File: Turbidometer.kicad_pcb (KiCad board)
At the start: 2 copper layers, 35 x 35 mm, 16 parts, among them IC1 BH1730FVC-TR, IC2 NLSX4373DR2G, J1 Conn_01x04, J2 Conn_01x04, U1 LP2985-3.0

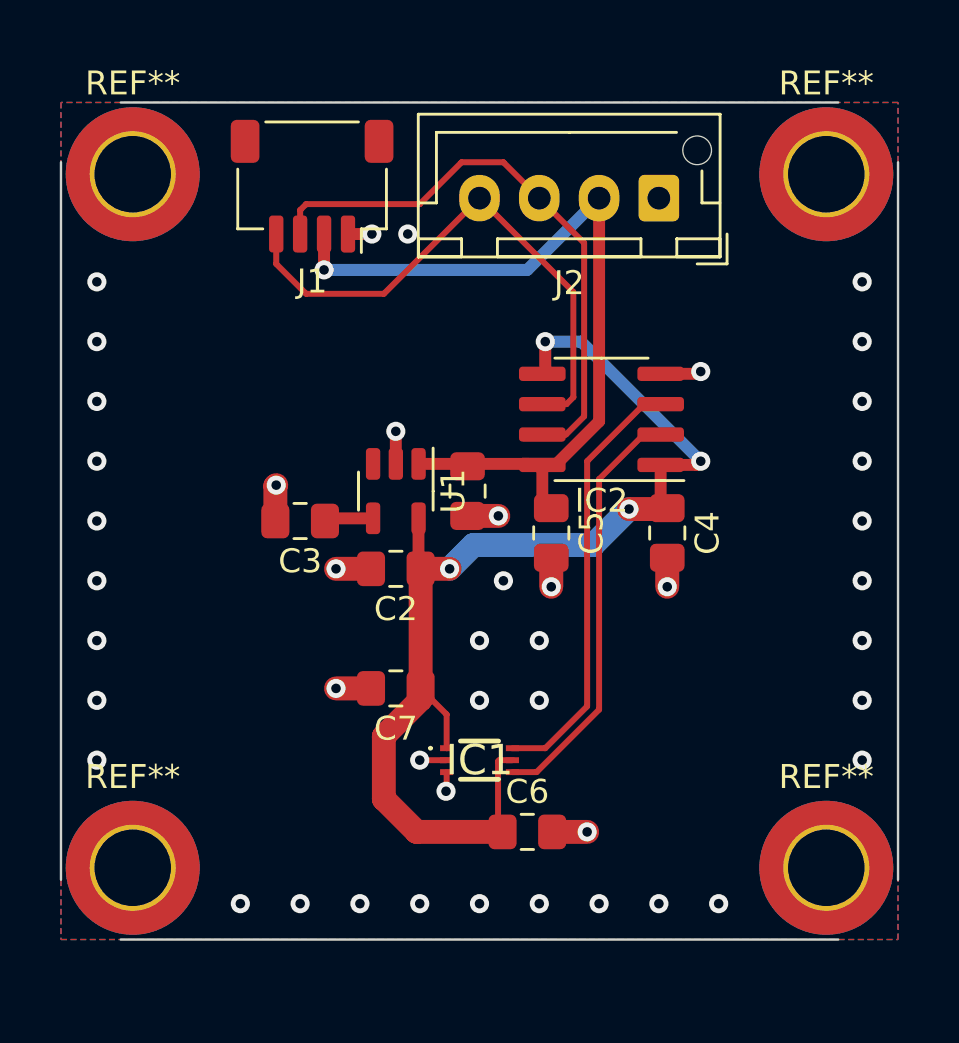
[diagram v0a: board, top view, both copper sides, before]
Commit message: Added missing tracks and several changes to satisfy ERC
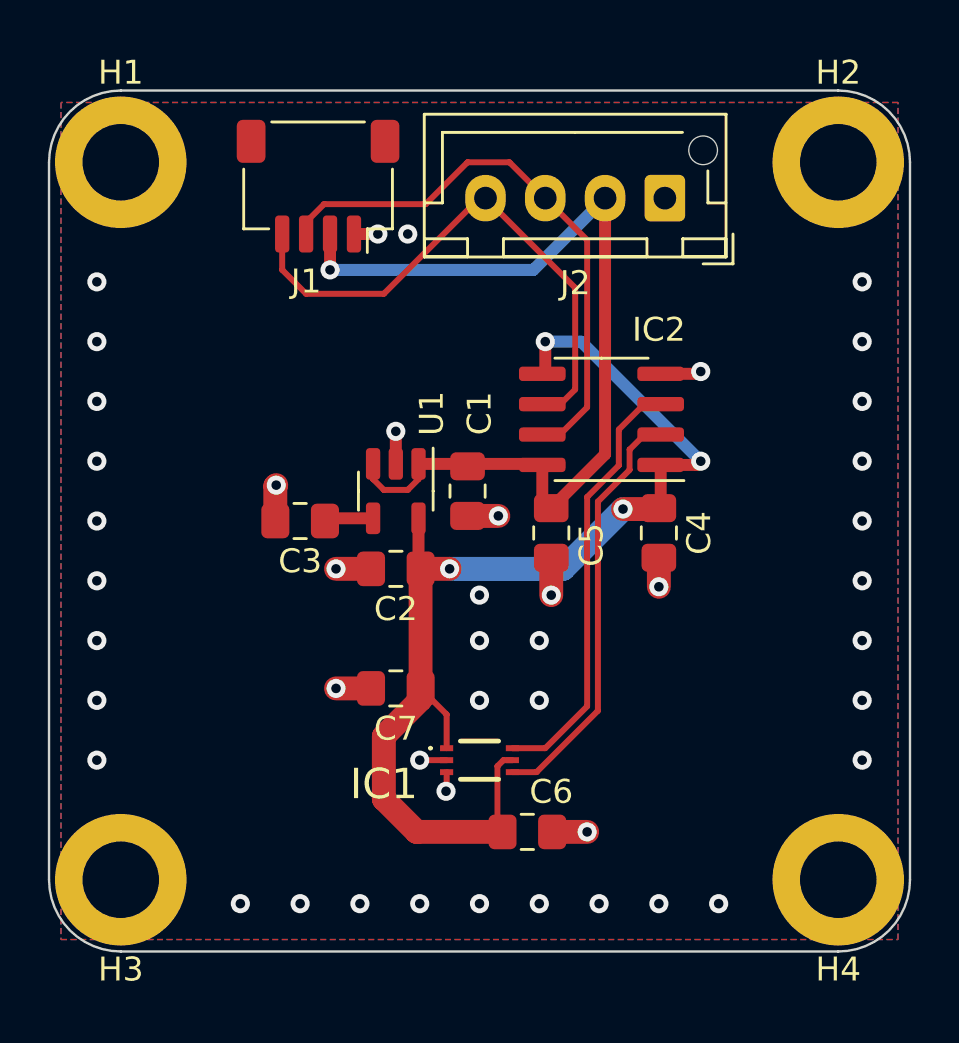
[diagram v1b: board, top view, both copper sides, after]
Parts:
- removed REF** (x4): MountingHole_3.2mm_M3_DIN965_Pad_TopBottom, MountingHole:MountingHole_3.2mm_M3_DIN965_Pad_TopBottom
- added H1: MountingHole, MountingHole:MountingHole_3.2mm_M3_ISO14580_Pad, F.Cu at (90.0, 47.5)
- added H2: MountingHole, MountingHole:MountingHole_3.2mm_M3_ISO14580_Pad, F.Cu at (120.0, 47.5)
- added H3: MountingHole, MountingHole:MountingHole_3.2mm_M3_ISO14580_Pad, F.Cu at (90.0, 77.5)
- added H4: MountingHole, MountingHole:MountingHole_3.2mm_M3_ISO14580_Pad, F.Cu at (120.0, 77.5)
- moved C4 0.35 mm to (112.5, 63.0)
- moved J1 0.25 mm to (98.2, 48.5)
- moved J2 0.25 mm to (112.8, 49.0)
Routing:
- net +3V3: track 33.9 -> 38.2 mm
- net SDA-VCC: track 24.4 -> 22.7 mm
- net SCL: track 18.6 -> 17.5 mm
- net +3V0: track 49.5 -> 48.4 mm
- net SCL-VCC: track 23.3 -> 22.2 mm
- net SDA: track 17.7 -> 17.0 mm
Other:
- board size 35 x 35 mm -> 36 x 36 mm
